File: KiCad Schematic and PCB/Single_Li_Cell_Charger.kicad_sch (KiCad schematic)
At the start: 13 parts, among them J1 USB_B_Micro, J2 VDD, J3 STAT, J4 PROG, J5 +BATT, J6 GND, U1 MCP73832T-2DCI/OT

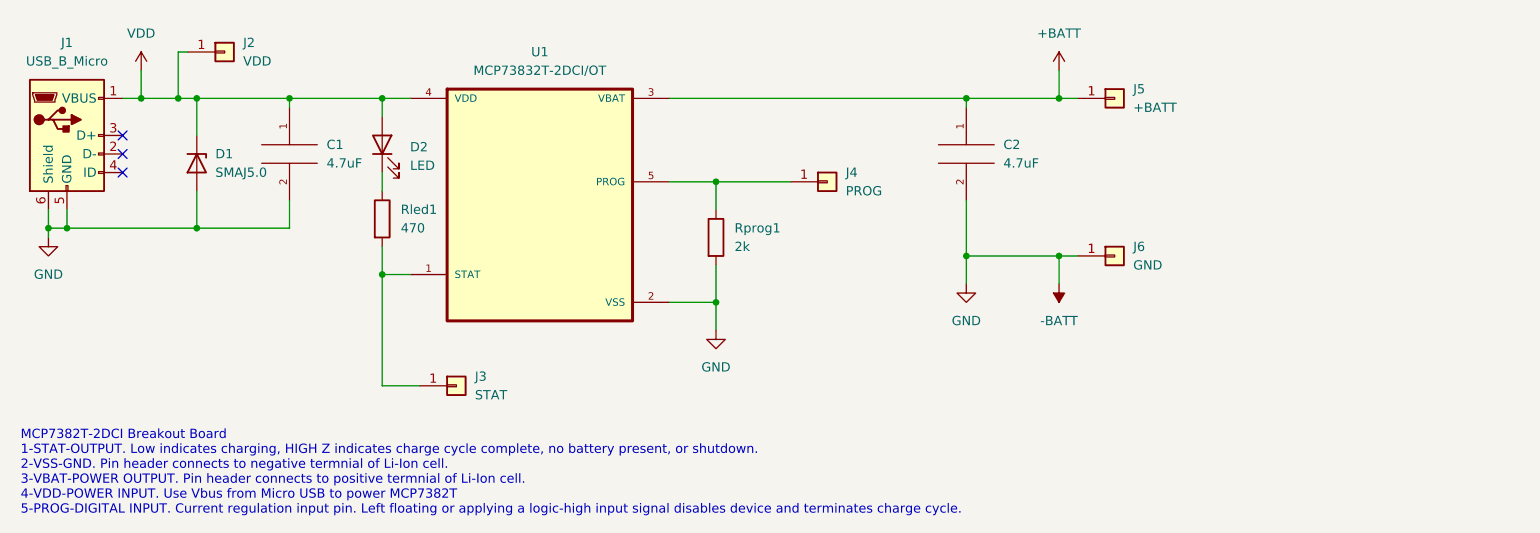
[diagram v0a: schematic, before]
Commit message: V2
V2- Updated MicroUSB footprint and changed header pins so it will fit a row of pin headers instead of them being spaced out.
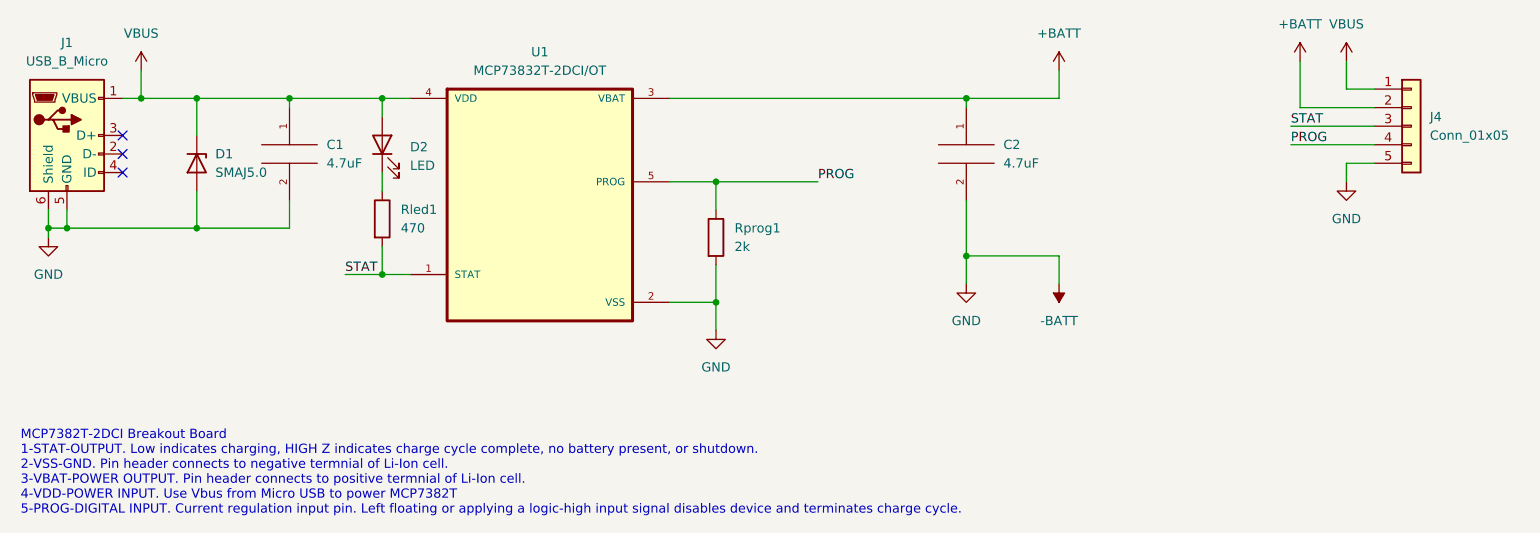
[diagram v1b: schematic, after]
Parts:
- removed J2: VDD, Connector_PinSocket_2.54mm:PinSocket_1x01_P2.54mm_Vertical, symbol Connector_Generic:Conn_01x01
- removed J3: STAT, Connector_PinSocket_2.54mm:PinSocket_1x01_P2.54mm_Vertical, symbol Connector_Generic:Conn_01x01
- removed J4: PROG, Connector_PinSocket_2.54mm:PinSocket_1x01_P2.54mm_Vertical, symbol Connector_Generic:Conn_01x01
- removed J5: +BATT, Connector_PinSocket_2.54mm:PinSocket_1x01_P2.54mm_Vertical, symbol Connector_Generic:Conn_01x01
- removed J6: GND, Connector_PinSocket_2.54mm:PinSocket_1x01_P2.54mm_Vertical, symbol Connector_Generic:Conn_01x01
- added J4: Conn_01x05, Connector_PinHeader_2.54mm:PinHeader_1x05_P2.54mm_Vertical, symbol Connector_Generic:Conn_01x05
- J1: footprint allied_connectors_usb:micro_usb_b_2.0_horizontal -> AMUSB464:micro_usb_b_2.0_horizontal
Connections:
- net +BATT: now also J4.2 (Pin_2)
- net -BATT: now also J4.5 (Pin_5)
- net PROG: now reaches Rprog1.1, U1.5 (PROG)
- net PROG: now also J4.4 (Pin_4)
- net STAT: now reaches Rled1.2, U1.1 (STAT)
- net STAT: now also J4.3 (Pin_3)
- net VDD renamed VBUS
- net VBUS: now also J4.1 (Pin_1)
